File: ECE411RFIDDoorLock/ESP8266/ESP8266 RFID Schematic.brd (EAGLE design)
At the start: 61 x 43.8 mm, 31 parts, among them J4 1050170001, M1 SERVO, Q3 MMBT2222ALT1GOSCT-ND, T1 600mA/40V, T2 600mA/40V, U1 CP2104, U2 AP2112K-3.3TRG1, X1 ESP-12E

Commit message: Final PCB draft
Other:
- board text added: "3.3v"
- board text added: "ECE 411 Team 12 Fall 2020 11/18/20 Authors: Miles Breslin, Miguel Higgins Moy, Noah Page, John Sharpe Revision E Adapted from Adafruit Feather Huzzah by Limor Fried/Ladyada for Adafruit Industries"
- board text removed: "ECE 411 Team 12 Fall 2020 Authors: Miles Breslin, Miguel Higgins Moy, Noah Page, John Sharpe Revision D Adapted from Adafruit Feather Huzzah by Limor Fried/Ladyada for Adafruit Industries"
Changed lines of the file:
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@@
 <layer number="25" name="tNames" color="7" fill="1" visible="yes" active="yes"/>
 <layer number="26" name="bNames" color="7" fill="1" visible="yes" active="yes"/>
-<layer number="27" name="tValues" color="7" fill="1" visible="yes" active="yes"/>
+<layer number="27" name="tValues" color="7" fill="1" visible="no" active="yes"/>
 <layer number="28" name="bValues" color="7" fill="1" visible="no" active="yes"/>
 <layer number="29" name="tStop" color="7" fill="3" visible="no" active="yes"/>
@@
 <layer number="35" name="tGlue" color="7" fill="4" visible="no" active="yes"/>
 <layer number="36" name="bGlue" color="7" fill="5" visible="no" active="yes"/>
-<layer number="37" name="tTest" color="7" fill="1" visible="yes" active="yes"/>
-<layer number="38" name="bTest" color="7" fill="1" visible="yes" active="yes"/>
+<layer number="37" name="tTest" color="7" fill="1" visible="no" active="yes"/>
+<layer number="38" name="bTest" color="7" fill="1" visible="no" active="yes"/>
 <layer number="39" name="tKeepout" color="4" fill="11" visible="yes" active="yes"/>
 <layer number="40" name="bKeepout" color="1" fill="11" visible="yes" active="yes"/>
@@
 <layer number="43" name="vRestrict" color="2" fill="10" visible="no" active="yes"/>
 <layer number="44" name="Drills" color="7" fill="1" visible="no" active="yes"/>
-<layer number="45" name="Holes" color="7" fill="1" visible="no" active="yes"/>
-<layer number="46" name="Milling" color="3" fill="1" visible="no" active="yes"/>
+<layer number="45" name="Holes" color="7" fill="1" visible="yes" active="yes"/>
+<layer number="46" name="Milling" color="3" fill="1" visible="yes" active="yes"/>
 <layer number="47" name="Measures" color="7" fill="1" visible="no" active="yes"/>
 <layer number="48" name="Document" color="7" fill="1" visible="no" active="yes"/>
@@
 <hole x="50.165" y="40.64" drill="3.2"/>
 <hole x="3.81" y="8.255" drill="3.2"/>
-<text x="17.78" y="8.89" size="1.016" layer="21">ECE 411 Team 12 Fall 2020
+<text x="17.78" y="8.89" size="1.016" layer="21">ECE 411 Team 12 Fall 2020 11/18/20
 Authors: Miles Breslin, Miguel Higgins Moy,
 Noah Page, John Sharpe
-                                                  Revision D
+                                                  Revision E
 Adapted from Adafruit Feather Huzzah by
 Limor Fried/Ladyada for Adafruit Industries</text>
@@
 <text x="58.42" y="30.353" size="0.4064" layer="21">ADC
 </text>
-<text x="2.921" y="4.318" size="2.1844" layer="21">--</text>
+<text x="2.286" y="4.318" size="2.1844" layer="21">--</text>
 <text x="5.969" y="8.509" size="0.8128" layer="21" distance="30" rot="R270">BATT
 MAX 6v
 ++</text>
-<text x="13.462" y="4.826" size="2.1844" layer="21" rot="R90">--</text>
-<text x="26.162" y="4.826" size="2.1844" layer="21" rot="R90">--</text>
-<text x="23.749" y="4.699" size="2.1844" layer="21" rot="R90">++</text>
-<text x="15.621" y="5.08" size="0.8128" layer="21" rot="R90">5 / SCL</text>
+<text x="13.335" y="4.826" size="1.6764" layer="21" rot="R90">--</text>
+<text x="26.035" y="4.953" size="1.778" layer="21" rot="R90">--</text>
+<text x="21.971" y="4.699" size="1.016" layer="21">++</text>
+<text x="15.875" y="5.08" size="0.8128" layer="21" rot="R90">5 / SCL</text>
 <text x="20.955" y="5.08" size="0.8128" layer="21" rot="R90">1
 SDA</text>
@@
 <text x="41.021" y="5.08" size="0.8128" layer="21" rot="R90">NC</text>
 <text x="43.561" y="5.08" size="0.8128" layer="21" rot="R90">GND</text>
-<text x="48.641" y="5.207" size="0.8128" layer="21" rot="R90">3.3</text>
+<text x="47.117" y="4.699" size="0.8128" layer="21">3.3v</text>
 <text x="46.101" y="5.08" size="0.8128" layer="21" rot="R90">NC</text>
 <text x="58.42" y="25.273" size="0.4064" layer="21">NC
@@
 </element>
 <element name="JP4" library="microbuilder" package="1X16_ROUND" value="" x="57.15" y="22.225" smashed="yes" rot="R90">
-<attribute name="NAME" x="59.1312" y="40.5638" size="0.8128" layer="25" ratio="18" rot="R90"/>
+<attribute name="NAME" x="59.1312" y="39.9288" size="0.8128" layer="25" ratio="18" rot="R90"/>
 <attribute name="VALUE" x="60.325" y="1.905" size="0.4064" layer="27" ratio="10" rot="R90"/>
 </element>
@@
 </element>
 <element name="R2" library="microbuilder" package="0603-MINI" value="1k" x="13.335" y="35.56" smashed="yes" rot="R180">
-<attribute name="NAME" x="13.0175" y="37.973" size="0.8128" layer="25" ratio="18" rot="R270"/>
+<attribute name="NAME" x="13.9065" y="37.973" size="0.8128" layer="25" ratio="18" rot="R270"/>
 <attribute name="VALUE" x="12.446" y="37.211" size="0.4064" layer="27" ratio="10" rot="R270"/>
 </element>
@@
 </element>
 <element name="U1" library="microbuilder" package="QFN24_4MM_SMSC" value="CP2104" x="9.017" y="29.845" smashed="yes">
-<attribute name="NAME" x="6.725" y="32.602" size="0.8128" layer="25" ratio="18" rot="R90"/>
+<attribute name="NAME" x="6.09" y="32.475" size="0.8128" layer="25" ratio="18" rot="R90"/>
 <attribute name="VALUE" x="7.787" y="32.41" size="0.4064" layer="27" ratio="10"/>
 </element>

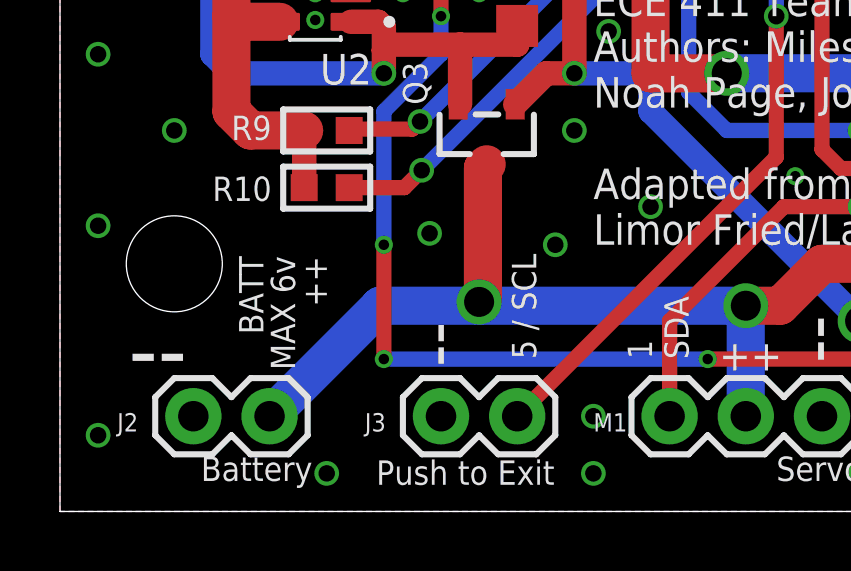
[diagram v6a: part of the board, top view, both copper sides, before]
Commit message: Added pull up resistor to push to exit
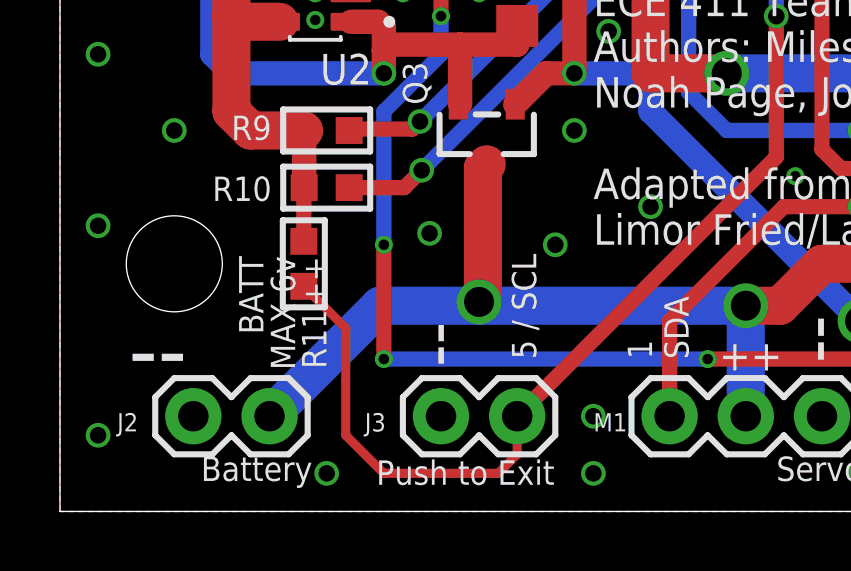
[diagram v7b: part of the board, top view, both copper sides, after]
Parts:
- added R11: 4.7k, microbuilder:0603-MINI
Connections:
- net 3.3V: now also R11.1
- net GPIO5/SCL: now also R11.2
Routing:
- net GPIO5/SCL: track 62.3 -> 75.6 mm
- net 3.3V: track 128.3 -> 130.1 mm

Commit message: Readme update and organizing
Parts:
- R11: value 4.7k -> 10k
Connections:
- new net N$4: R9.1, X1.3
- net CH_PD: no longer R9.1, X1.3
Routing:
- net GPIO5/SCL: track 75.6 -> 62.1 mm
- net CH_PD: track 74.2 -> 71.7 mm
